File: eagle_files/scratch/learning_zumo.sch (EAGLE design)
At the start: 23 parts

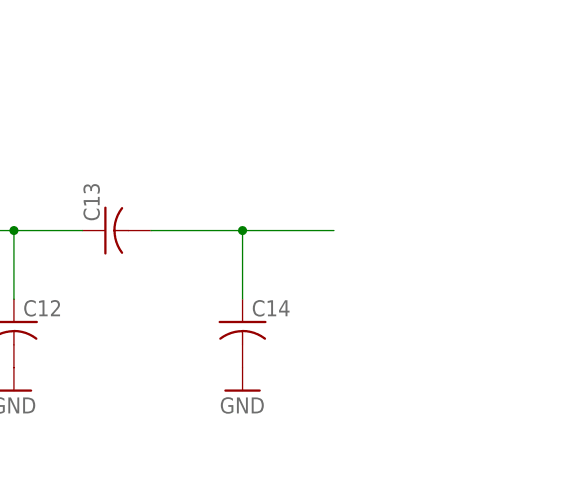
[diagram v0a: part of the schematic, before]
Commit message: refined newest board design, adding debugger pinout locals
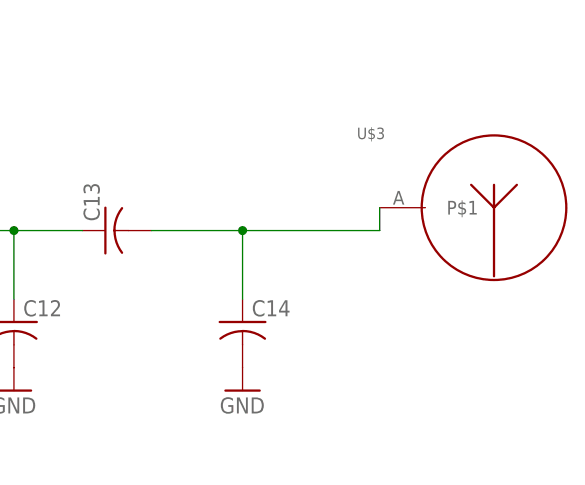
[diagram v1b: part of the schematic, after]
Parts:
- added U$3: ANTENNA, CC1310F128RGZT:ANTENNA
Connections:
- net N$16: now also U$3.P$1
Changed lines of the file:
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@@
 <part name="GND8" library="Swarm" deviceset="GND" device=""/>
 <part name="GND9" library="Swarm" deviceset="GND" device=""/>
+<part name="U$3" library="CC1310F128RGZT" deviceset="ANTENNA" device=""/>
 </parts>
 <sheets>
@@
 <instance part="GND9" gate="1" x="325.12" y="53.34" smashed="yes">
 <attribute name="VALUE" x="322.58" y="50.8" size="1.778" layer="96"/>
+</instance>
+<instance part="U$3" gate="G$1" x="345.44" y="73.66" smashed="yes">
+<attribute name="NAME" x="337.82" y="81.28" size="1.27" layer="95"/>
 </instance>
 </instances>
@@
 <pinref part="C14" gate="G$1" pin="1"/>
 <wire x1="325.12" y1="71.12" x2="325.12" y2="63.5" width="0.1524" layer="91"/>
-<wire x1="325.12" y1="71.12" x2="335.28" y2="71.12" width="0.1524" layer="91"/>
+<wire x1="325.12" y1="71.12" x2="340.36" y2="71.12" width="0.1524" layer="91"/>
 <junction x="325.12" y="71.12"/>
-</segment>
-</net>
+<pinref part="U$3" gate="G$1" pin="P$1"/>
+<wire x1="340.36" y1="71.12" x2="340.36" y2="73.66" width="0.1524" layer="91"/>
+</segment>
+</net>

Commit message: days worth of work, added a bunch of componenets to the libraries, gave the power considerations a first take, began implementing the board, implement motor driver circuitry
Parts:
- added C15, C16, C17: (no value), Swarm:CPOL-USE2.5-6
- added C18: 34nF, Swarm:C-USC0805
- added C19, C20, C21, C22, C24, C25: 100nF, Swarm:C-USC0805
- added C23: 22uF, Swarm:C-USC0805
- added C26, C27, C28, C29, C30, C31: 1nF, Swarm:C-USC0805
- added C32, C33: 3.3nF, Swarm:C-USC0805
- added CL, CR, EL, ER, ML, MR: IR_LED, Swarm:IR_LED
- added L6: 6.8uH, Swarm:L-US0204/7
- added R2, R3, R4, R5, R6, R7, R8, R9: 220, Swarm:R-US_R0805
- added S1: (no value), Swarm:MOMENTARY-SWITCH-SPST-2-SMD-4.6X2.8MM
- added U$10, U$9: 20MM_COINCELL, Swarm:20MM_COINCELL
- added U$4: DEBUG_BREAKOUT, CC1310F128RGZ:DEBUG_BREAKOUT
- added U$5: DRV8835DRV8835, Swarm:DRV8835DRV8835
- added U$6: SWITCH_JS202011SCQN, Swarm:SWITCH_JS202011SCQN
- added U$7, U$8: DC_MOTOR, Swarm:DC_MOTOR
- added U1: 5v, Swarm:NU32V7_V_REG_LM1117SOT223
- added U2: 3v3, Swarm:NU32V7_V_REG_LM1117SOT223
- C1, C10, C11, C12, C13, C14, C2, C3, C4, C5, C6, C7, C8, C9: device Swarm:C-US025-024X044 -> Swarm:C-USC0805
- R1: device Swarm:R-US_0204/7 -> Swarm:R-US_R0805
- U$3: device CC1310F128RGZT:ANTENNA -> CC1310F128RGZ:ANTENNA
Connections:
- removed net N$6: U$1.DIO28
- new net 3V3: C17.+, U$5.VCC, U$6.CA, U2.OUT, U2.OUT@1
- new net 5V: C16.+, C26.1, C27.1, C28.1, C29.1, C30.1, C31.1, U$5.MODE, U1.OUT, U1.OUT@1, U2.IN
- new net DCDC_SW: L6.1, U$1.DCDC_SW
- new net IR_CL: R5.1, U$1.DIO24
- new net IR_CR: R9.1, U$1.DIO23
- new net IR_EL: R3.1, U$1.DIO28
- new net IR_ER: R7.1, U$1.DIO27
- new net IR_ML: R4.1, U$1.DIO26
- new net IR_MR: R8.1, U$1.DIO25
- new net JTAG_TDI: U$1.DIO17, U$4.TDI
- new net JTAG_TDO: U$1.DIO16, U$4.TDO
- new net M1DIR: U$1.DIO20, U$5.APHASE
- new net M1PWM: U$1.DIO11, U$5.AENBL
- new net M2DIR: U$1.DIO19, U$5.BPHASE
- new net M2PWM: U$1.DIO12, U$5.BENBL
- new net N$17: ER.1.AN, R6.1
- new net N$18: EL.1.AN, R2.1
- new net N$19: C26.2, EL.3.CO, R3.2
- new net N$20: EL.2.CA, ML.1.AN
- new net N$21: CL.1.AN, ML.2.CA
- new net N$22: U$1.DIO21
- new net N$23: C27.2, ML.3.CO, R4.2
- new net N$24: C33.2, U$5.BOUT+, U$7.+
- new net N$25: C33.1, U$5.BOUT-, U$7.-
- new net N$26: C32.2, U$5.AOUT+, U$8.+
- new net N$27: C32.1, U$5.AOUT-, U$8.-
- new net N$28: C28.2, CL.3.CO, R5.2
- new net N$29: C29.2, ER.3.CO, R7.2
- new net N$30: ER.2.CA, MR.1.AN
- new net N$31: CR.1.AN, MR.2.CA
- new net N$33: C30.2, MR.3.CO, R8.2
- new net N$34: C31.2, CR.3.CO, R9.2
- new net VBAT: C15.+, R2.2, R6.2, U$5.VM, U$9.1.POS, U$9.2.POS, U1.IN
- net GND: now also C10.2, C15.-, C16.-, C17.-, C18.2, C19.2, C20.2, C21.2, C22.2, C23.2, C24.2, C25.2, C5.1, C8.2, C9.2, CL.2.CA, CL.4.EM, CR.2.CA, CR.4.EM, EL.4.EM, ER.4.EM, ML.4.EM, MR.4.EM, S1.3, U$10.3.GND, U$4.GND, U$5.GND, U$5.GND2, U1.ADJ, U2.ADJ
- net JTAG_TCK: now also U$4.TCK
- net JTAG_TMS: now also U$4.TMS
- net N$1: no longer U$1.DCDC_SW
- net N$2: no longer U$1.DIO19, U$1.DIO20, U$1.DIO21, U$1.DIO23, U$1.DIO24, U$1.DIO25, U$1.DIO26
- net N$4: no longer U$1.DIO11, U$1.DIO12, U$1.DIO16, U$1.DIO17
- net N$5: now also U$10.1.POS, U$10.2.POS, U$9.3.GND; no longer U$1.DIO27
- net N_RESET: now also S1.1, U$4.RESET
- net VDDR: now also C23.1, C24.1, C25.1, L6.2
- net VDDS: now also C18.1, C19.1, C20.1, C21.1, C22.1, U$6.2_A
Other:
- moved on the sheet: U$3

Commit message: figuring last details on antenna balun
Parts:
- added FB: FERRITE_BEAD, CC1310F128RGZ:FERRITE_BEAD
- C1: value 0,1uF -> 100nF; device Swarm:C-USC0805 -> learning_particle:C-US
- C10, C18, C19, C2, C20, C21, C22, C23, C24, C25, C3, C4, C5, C6, C7, C8, C9: device Swarm:C-USC0805 -> learning_particle:C-US
- C11: value (none) -> 100pF; device Swarm:C-USC0805 -> learning_particle:C-US
- C12, C14: value (none) -> DNM; device Swarm:C-USC0805 -> learning_particle:C-US
- C13: value (none) -> 1.8pF; device Swarm:C-USC0805 -> learning_particle:C-US
- L1, L2, L3, L4, L5, L6: device Swarm:L-US0204/7 -> learning_particle:L-US
- U$1: device CC1310F128RGZT:CC1310 -> learning_particle:CC1310
- renumbered 32KHZ to Y2, U$2 to Y1, U$4 to DEBUG_HEADER, U$5 to DRV8835, U$6 to PW_SW, U$7 to M2, U$8 to M1, U1 to 5V_REG, U2 to 3V3_REG
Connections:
- net N$11 renamed X_48_Q2
- removed net N$10: C7.1, L3.2, U$1.RX_TX
- removed net N$13: C9.1, L4.2, L5.1
- removed net N$14: C10.1, C11.1, L5.2
- removed net N$15: C11.2, C12.1, C13.1
- removed net N$16: C13.2, C14.1, U$3.P$1
- removed net N$22: U$1.DIO21
- removed net N$8: U$1.DIO30
- removed net N$9: C4.1, U$1.X32K_Q2, Y2.Q2
- new net N$6: C11.P$2, C12.P$1, C13.P$1
- new net RF_N: C6.P$1, L1.2, L3.1, U$1.RF_N
- new net RF_P: C5.P$2, L1.1, L2.1, U$1.RF_P
- new net RF_TX: C7.P$1, L3.2, U$1.RX_TX
- new net X32_Q1: C2.P$1, U$1.X32K_Q1, Y2.Q1
- new net X32_Q2: C4.P$1, U$1.X32K_Q2, Y2.Q2
- new net X_48_Q1: U$1.X48M_N, Y1.3.Q2
- net GND: now also C1.P$2, C10.P$2, C12.P$2, C14.P$2, C18.P$2, C19.P$2, C2.P$2, C20.P$2, C21.P$2, C22.P$2, C23.P$2, C24.P$2, C25.P$2, C3.P$2, C4.P$2, C5.P$1, C7.P$2, C8.P$2, C9.P$2; no longer C1.2, C10.2, C12.2, C14.2, C18.2, C19.2, C2.2, C20.2, C21.2, C22.2, C23.2, C24.2, C25.2, C3.2, C4.2, C5.1, C7.2, C8.2, C9.2
- net N$1: now also C3.P$1; no longer C2.1, C3.1, U$1.DIO1, U$1.DIO2, U$1.DIO3, U$1.DIO4, U$1.DIO5, U$1.DIO6, U$1.DIO7, U$1.DIO8, U$1.DIO9, U$1.X32K_Q1, Y2.Q1
- net N$12: now also C6.P$2, C8.P$1; no longer C6.2, C8.1
- net N$2: now also C9.P$1, L4.2, L5.1; no longer C5.2, C6.1, L1.1, L1.2, L2.1, L3.1, U$1.DIO18, U$1.DIO22, U$1.RF_N, U$1.RF_P, U$1.X48M_N, Y1.3.Q2
- net N$3: now also C10.P$1, C11.P$1, L5.2; no longer U$1.DIO10
- net N$4: now also FB.1, PW_SW.2_A; no longer U$1.DIO13, U$1.DIO14, U$1.DIO15
- net N$7: now also C13.P$2, C14.P$1, U$3.P$1; no longer U$1.DIO29
- net N_RESET: now also C1.P$1; no longer C1.1
- net VDDR: now also C23.P$1, C24.P$1, C25.P$1; no longer C23.1, C24.1, C25.1
- net VDDS: now also C18.P$1, C19.P$1, C20.P$1, C21.P$1, C22.P$1, FB.2; no longer C18.1, C19.1, C20.1, C21.1, C22.1, PW_SW.2_A
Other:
- moved on the sheet: C1, C10, C11, C12, C13, C14, C18, C19, C2, C20, C21, C22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

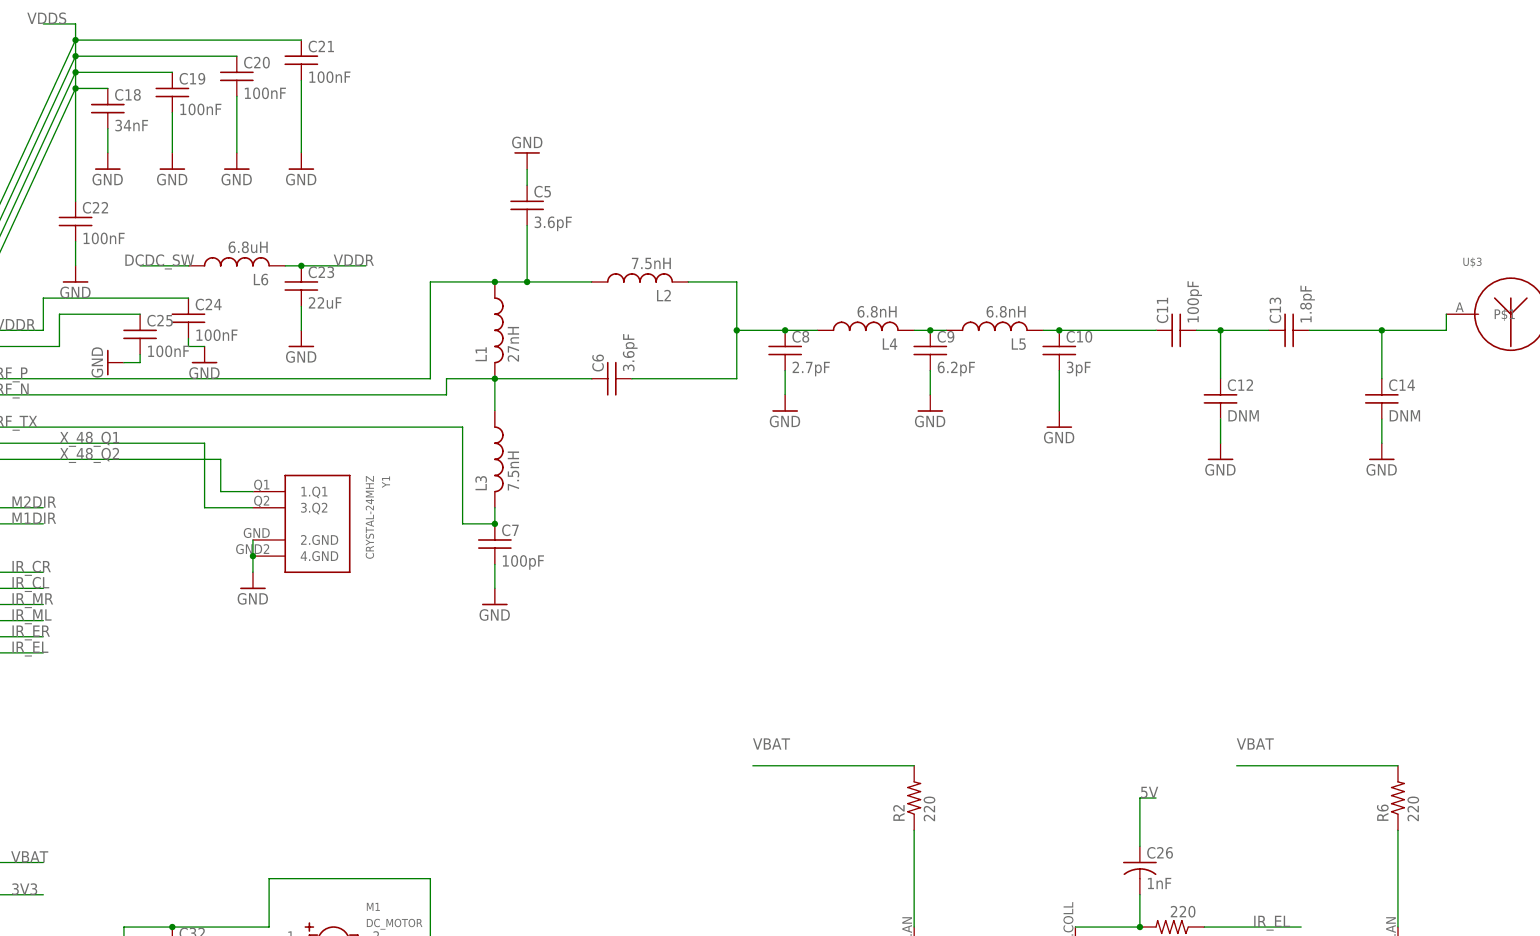
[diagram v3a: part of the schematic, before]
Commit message: most updated, finished balun and other minimum reqs for CC1310, working on integrating battery motor driver and sensors
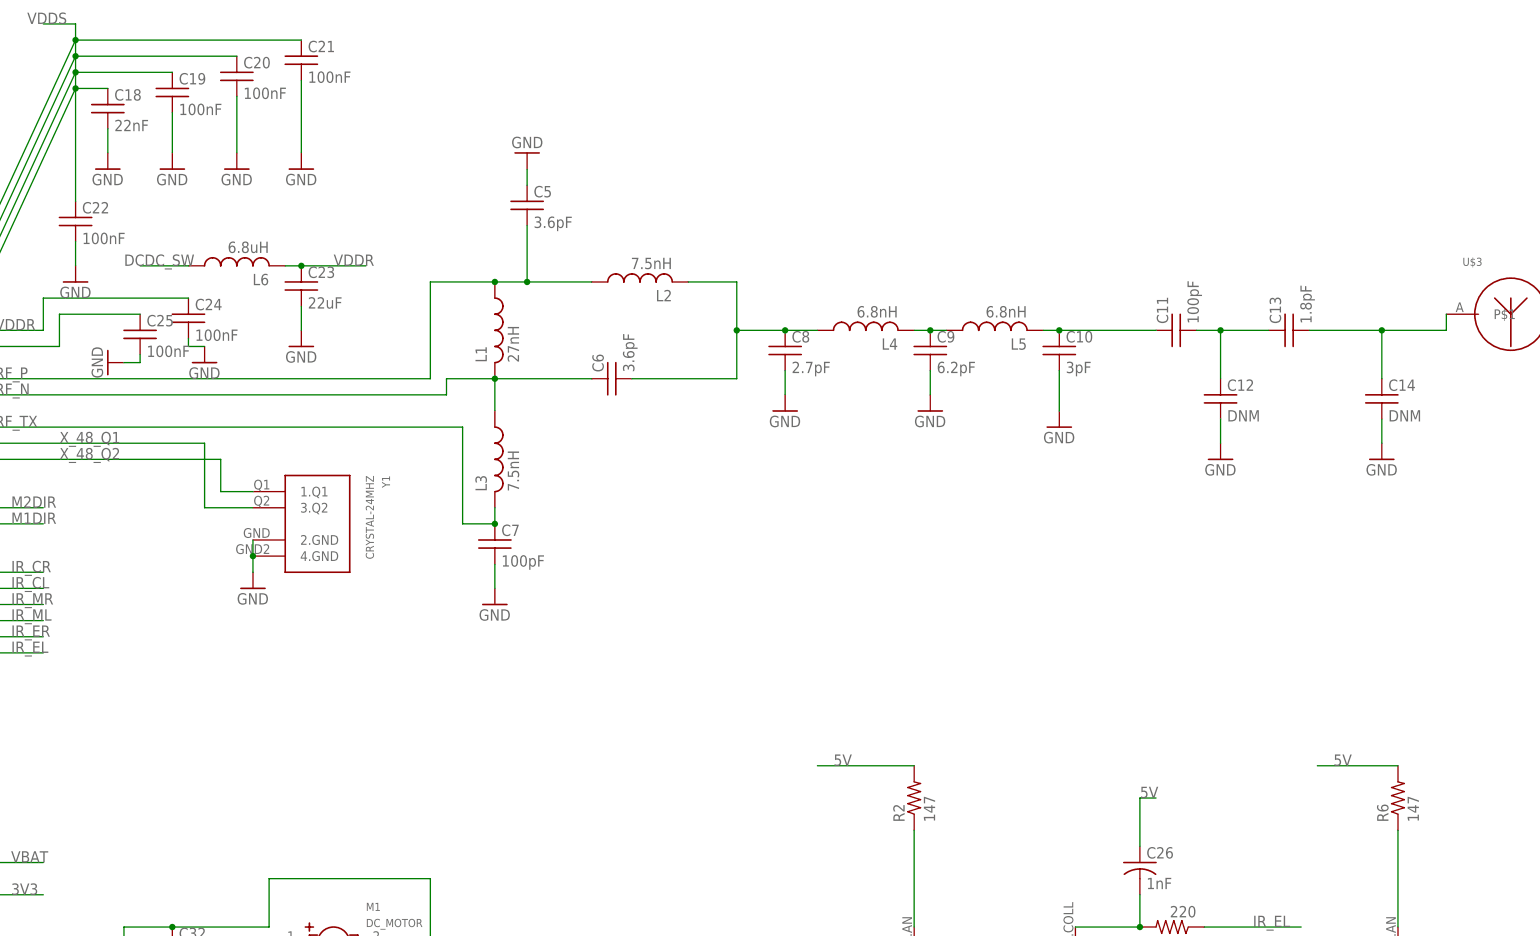
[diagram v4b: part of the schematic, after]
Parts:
- C18: value 34nF -> 22nF
- R1: device Swarm:R-US_R0805 -> learning_particle:R-US"
- R2, R6: value 220 -> 147
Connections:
- net 5V: now also R2.2, R6.2
- net VBAT: no longer R2.2, R6.2
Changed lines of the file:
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@@
 <parts>
 <part name="U$1" library="learning_particle" deviceset="CC1310" device=""/>
-<part name="R1" library="Swarm" deviceset="R-US_" device="R0805" package3d_urn="urn:adsk.eagle:package:23553/2" value="100K"/>
+<part name="R1" library="learning_particle" deviceset="R-US" device="&quot;" value="100K"/>
 <part name="C1" library="learning_particle" deviceset="C-US" device="" value="100nF"/>
 <part name="GND1" library="Swarm" deviceset="GND" device=""/>
@@
 <part name="C17" library="Swarm" deviceset="CPOL-US" device="E2.5-6" package3d_urn="urn:adsk.eagle:package:23349/1"/>
 <part name="GND16" library="Swarm" deviceset="GND" device=""/>
-<part name="C18" library="learning_particle" deviceset="C-US" device="" value="34nF"/>
+<part name="C18" library="learning_particle" deviceset="C-US" device="" value="22nF"/>
 <part name="C19" library="learning_particle" deviceset="C-US" device="" value="100nF"/>
 <part name="C20" library="learning_particle" deviceset="C-US" device="" value="100nF"/>
@@
 <part name="GND24" library="Swarm" deviceset="GND" device=""/>
 <part name="PW_SW" library="Swarm" deviceset="SWITCH_JS202011SCQN" device=""/>
-<part name="R2" library="Swarm" deviceset="R-US_" device="R0805" package3d_urn="urn:adsk.eagle:package:23553/2" value="220"/>
+<part name="R2" library="Swarm" deviceset="R-US_" device="R0805" package3d_urn="urn:adsk.eagle:package:23553/2" value="147"/>
 <part name="GND25" library="Swarm" deviceset="GND" device=""/>
 <part name="GND26" library="Swarm" deviceset="GND" device=""/>
@@
 <part name="ML" library="Swarm" deviceset="IR_LED" device=""/>
 <part name="CL" library="Swarm" deviceset="IR_LED" device=""/>
-<part name="R6" library="Swarm" deviceset="R-US_" device="R0805" package3d_urn="urn:adsk.eagle:package:23553/2" value="220"/>
+<part name="R6" library="Swarm" deviceset="R-US_" device="R0805" package3d_urn="urn:adsk.eagle:package:23553/2" value="147"/>
 <part name="GND28" library="Swarm" deviceset="GND" device=""/>
 <part name="GND29" library="Swarm" deviceset="GND" device=""/>
@@
 <label x="363.22" y="-2.54" size="1.778" layer="95"/>
 </segment>
+<segment>
+<pinref part="R2" gate="G$1" pin="2"/>
+<wire x1="251.46" y1="2.54" x2="236.22" y2="2.54" width="0.1524" layer="91"/>
+<label x="238.76" y="2.54" size="1.778" layer="95"/>
+</segment>
+<segment>
+<pinref part="R6" gate="G$1" pin="2"/>
+<wire x1="327.66" y1="2.54" x2="314.96" y2="2.54" width="0.1524" layer="91"/>
+<label x="317.5" y="2.54" size="1.778" layer="95"/>
+</segment>
 </net>
 <net name="N$24" class="0">
@@
 </segment>
 <segment>
-<wire x1="226.06" y1="2.54" x2="251.46" y2="2.54" width="0.1524" layer="91"/>
-<pinref part="R2" gate="G$1" pin="2"/>
-<label x="226.06" y="5.08" size="1.778" layer="95"/>
-</segment>
-<segment>
-<wire x1="302.26" y1="2.54" x2="327.66" y2="2.54" width="0.1524" layer="91"/>
-<pinref part="R6" gate="G$1" pin="2"/>
-<label x="302.26" y="5.08" size="1.778" layer="95"/>
-</segment>
-<segment>

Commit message: finished up iteration 1 of the board!
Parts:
- removed C16, C17: (no value), Swarm:CPOL-USE2.5-6
- added U$2: GP2Y_DIST_SENSE_BREAKOUT, learning_particle:GP2Y_DIST_SENSE_BREAKOUT
- DRV8835: device Swarm:DRV8835DRV8835 -> learning_particle:DRV8835DRV8835
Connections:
- new net DIST0: U$1.DIO29, U$2.SIG
- new net N$9: U$1.DIO30
- net 3V3: now also U$2.VCC; no longer C17.+
- net 5V: no longer C16.+
- net GND: now also U$2.GND; no longer C16.-, C17.-
- net IR_CL: now also U$1.DIO26; no longer U$1.DIO24
- net IR_ER: now also U$1.DIO25; no longer U$1.DIO27
- net IR_ML: now also U$1.DIO27; no longer U$1.DIO26
- net IR_MR: now also U$1.DIO24; no longer U$1.DIO25

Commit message: finialized board pre submitting, added vias between top and bottom trace of antenna
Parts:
- M1, M2: device Swarm:DC_MOTOR -> learning_particle:DC_MOTOR
- U$10, U$9: device Swarm:20MM_COINCELL -> learning_particle:20MM_COINCELL
- U$3: device CC1310F128RGZ:ANTENNA -> learning_particle:ANTENNA
- Y1: device Swarm:CRYSTAL-24MHZ -> learning_particle:CRYSTAL-24MHZ
- Y2: device Swarm:CRYSTAL-32KHZ -> learning_particle:CRYSTAL-32KHZ
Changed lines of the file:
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@@
 <part name="C3" library="learning_particle" deviceset="C-US" device="" value="1uF"/>
 <part name="GND3" library="Swarm" deviceset="GND" device=""/>
-<part name="Y2" library="Swarm" deviceset="CRYSTAL-32KHZ" device=""/>
+<part name="Y2" library="learning_particle" deviceset="CRYSTAL-32KHZ" device=""/>
 <part name="C2" library="learning_particle" deviceset="C-US" device="" value="12pF"/>
 <part name="C4" library="learning_particle" deviceset="C-US" device="" value="12pF"/>
@@
 <part name="GND5" library="Swarm" deviceset="GND" device=""/>
 <part name="GND6" library="Swarm" deviceset="GND" device=""/>
-<part name="Y1" library="Swarm" deviceset="CRYSTAL-24MHZ" device=""/>
+<part name="Y1" library="learning_particle" deviceset="CRYSTAL-24MHZ" device=""/>
 <part name="L1" library="learning_particle" deviceset="L-US" device="" value="27nH"/>
 <part name="C5" library="learning_particle" deviceset="C-US" device="" value="3.6pF"/>
@@
 <part name="GND8" library="Swarm" deviceset="GND" device=""/>
 <part name="GND9" library="Swarm" deviceset="GND" device=""/>
-<part name="U$3" library="CC1310F128RGZ" deviceset="ANTENNA" device=""/>
+<part name="U$3" library="learning_particle" deviceset="ANTENNA" device=""/>
 <part name="DEBUG_HEADER" library="CC1310F128RGZ" deviceset="DEBUG_BREAKOUT" device=""/>
 <part name="GND10" library="Swarm" deviceset="GND" device=""/>
@@
 <part name="C32" library="Swarm" deviceset="C-US" device="C0805" package3d_urn="urn:adsk.eagle:package:23617/2" value="3.3nF"/>
 <part name="C33" library="Swarm" deviceset="C-US" device="C0805" package3d_urn="urn:adsk.eagle:package:23617/2" value="3.3nF"/>
-<part name="M2" library="Swarm" deviceset="DC_MOTOR" device=""/>
-<part name="M1" library="Swarm" deviceset="DC_MOTOR" device=""/>
+<part name="M2" library="learning_particle" deviceset="DC_MOTOR" device=""/>
+<part name="M1" library="learning_particle" deviceset="DC_MOTOR" device=""/>
 <part name="S1" library="Swarm" deviceset="MOMENTARY-SWITCH-SPST-2" device="-SMD-4.6X2.8MM"/>
 <part name="GND32" library="Swarm" deviceset="GND" device=""/>
@@
 <part name="GND35" library="Swarm" deviceset="GND" device=""/>
 <part name="GND36" library="Swarm" deviceset="GND" device=""/>
-<part name="U$9" library="Swarm" deviceset="20MM_COINCELL" device=""/>
-<part name="U$10" library="Swarm" deviceset="20MM_COINCELL" device=""/>
+<part name="U$9" library="learning_particle" deviceset="20MM_COINCELL" device=""/>
+<part name="U$10" library="learning_particle" deviceset="20MM_COINCELL" device=""/>
 <part name="GND37" library="Swarm" deviceset="GND" device=""/>
 <part name="FB" library="CC1310F128RGZ" deviceset="FERRITE_BEAD" device=""/>
@@
 <pinref part="C13" gate="G$1" pin="P$2"/>
 <wire x1="313.69" y1="71.12" x2="325.12" y2="71.12" width="0.1524" layer="91"/>
-<pinref part="U$3" gate="G$1" pin="P$1"/>
-<wire x1="325.12" y1="71.12" x2="335.28" y2="71.12" width="0.1524" layer="91"/>
-<wire x1="335.28" y1="71.12" x2="335.28" y2="73.66" width="0.1524" layer="91"/>
 <pinref part="C14" gate="G$1" pin="P$1"/>
 <wire x1="325.12" y1="63.5" x2="325.12" y2="71.12" width="0.1524" layer="91"/>
+<pinref part="U$3" gate="G$1" pin="P$1"/>
+<wire x1="325.12" y1="71.12" x2="325.12" y2="76.2" width="0.1524" layer="91"/>
+<wire x1="325.12" y1="76.2" x2="335.28" y2="76.2" width="0.1524" layer="91"/>
 <junction x="325.12" y="71.12"/>
 </segment>

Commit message: latest WORKING version of board and schematic
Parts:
- removed C15: (no value), Swarm:CPOL-USE2.5-6
- added DIST_1: GP2Y_DIST_SENSE_BREAKOUT, learning_particle:GP2Y_DIST_SENSE_BREAKOUT
- L6: device learning_particle:L-US -> learning_particle:L-USL0805
- renumbered U$2 to DIST_0
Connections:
- removed net N$9: U$1.DIO30
- new net DIST_1: DIST_1.SIG, U$1.DIO30
- net 3V3: now also DIST_1.VCC, FB.1; no longer PW_SW.CA
- net GND: now also DIST_1.GND; no longer C15.-
- net N$4: now also 5V_REG.IN; no longer FB.1
- net VBAT: now also PW_SW.CA; no longer 5V_REG.IN, C15.+
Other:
- moved on the sheet: FB
